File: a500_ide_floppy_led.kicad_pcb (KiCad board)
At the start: 2 copper layers, 20.5 x 11.7 mm, 6 parts, among them J1 Motherboard, J2 Keyboard, J3 ~{IDE_ACTIVITY}, Q1 2N3906

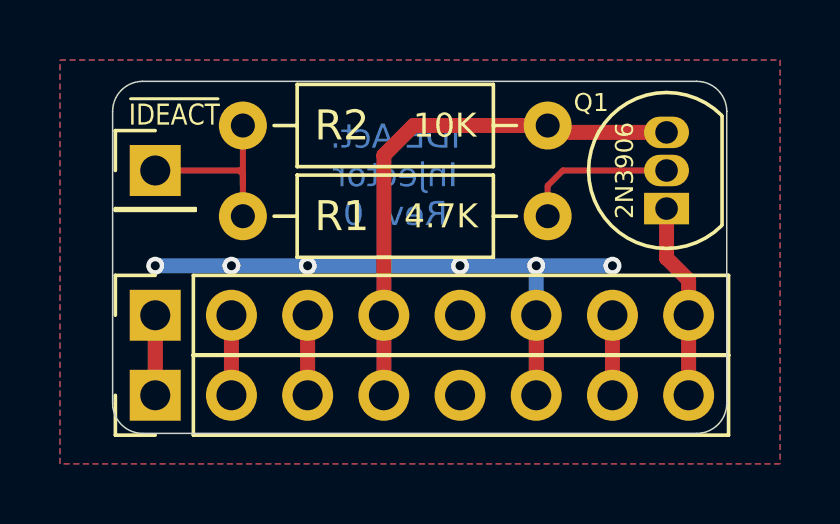
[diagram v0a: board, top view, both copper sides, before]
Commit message: Add untested rev.1 that buffers the signal
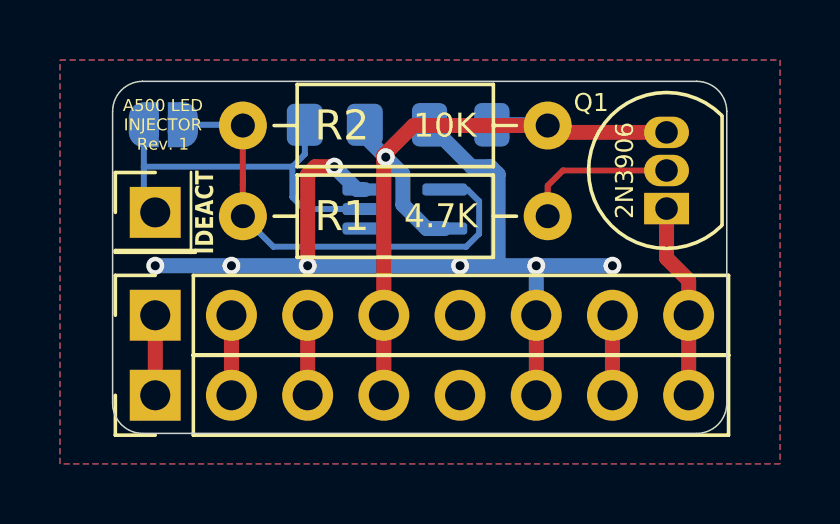
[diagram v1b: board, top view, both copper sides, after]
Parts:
- added C1: 100nF, Capacitor_SMD:C_0805_2012Metric_Pad1.18x1.45mm_HandSolder, B.Cu at (112.4, 22.5)
- added JP1: Buffer Bypass, Jumper:SolderJumper-2_P1.3mm_Open_RoundedPad1.0x1.5mm, B.Cu at (102.5, 22.5)
- added R3: 10K, Resistor_SMD:R_0805_2012Metric_Pad1.20x1.40mm_HandSolder, B.Cu at (108.2, 22.5)
- added U1: 74AHCT1G07, Package_TO_SOT_SMD:SOT-353_SC-70-5_Handsoldering, B.Cu at (110.6, 25.3)
- moved J3 1.40 mm to (102.2, 25.4)
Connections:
- R1 pad 1: Net-(J3-Pin_1) -> Net-(JP1-A)
- R2 pad 2: Net-(J3-Pin_1) -> Net-(JP1-A)
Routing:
- net Net-(JP1-A): track 0.00 -> 16.3 mm
- net GND: track 19.6 -> 31.0 mm, vias 6 -> 7
- net Net-(J3-Pin_1): track 6.35 -> 13.2 mm
- net VCC: track 18.6 -> 25.4 mm, vias 0 -> 1
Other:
- board text added: "A500 LED INJECTOR Rev. 1"
- board text removed: "IDE Act. Injector Rev. 0"
